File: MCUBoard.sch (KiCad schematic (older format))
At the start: 25 parts

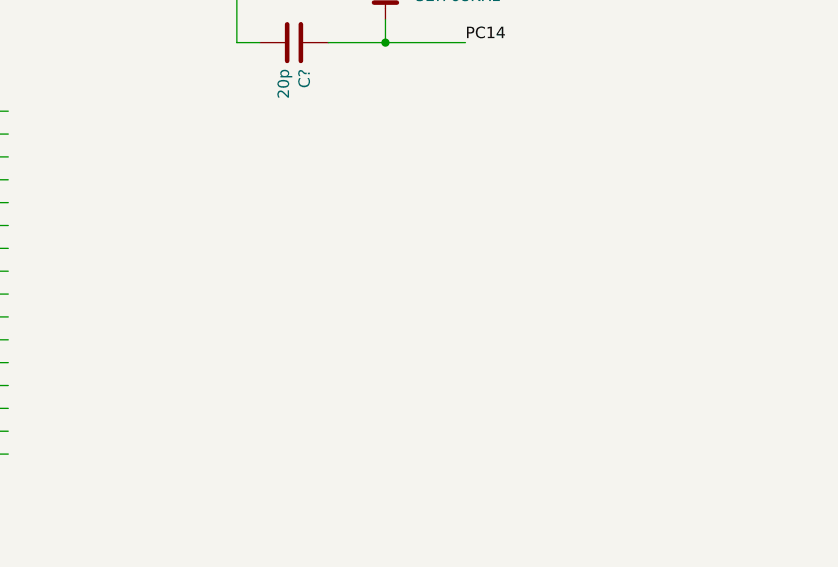
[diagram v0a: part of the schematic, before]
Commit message: added LDO to convert 5v to 3.3v
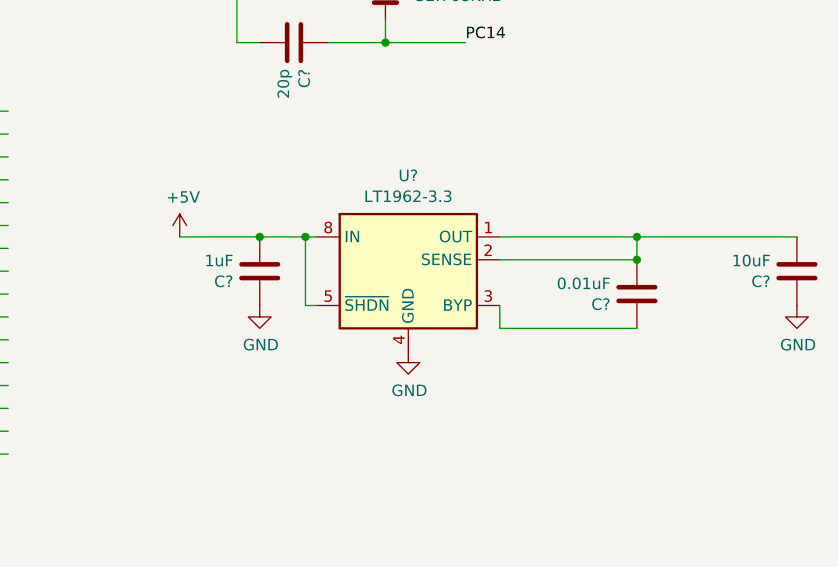
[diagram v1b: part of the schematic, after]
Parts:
- added C?: 0.01uF, symbol Device:C
- added C?: 10uF, symbol Device:C
- added C?: 1uF, symbol Device:C
- added U?: LT1962-3.3, Package_SO:MSOP-8_3x3mm_P0.65mm, symbol Regulator_Linear:LT1962-3.3
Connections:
- wire segments 105 -> 116
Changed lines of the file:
@@
 Wire Wire Line
 	1150 6400 1700 6400
+$Comp
+L Regulator_Linear:LT1962-3.3 U?
+U 1 1 5BB1DF66
+P 8250 3950
+F 0 "U?" H 8250 4417 50  0000 C CNN
+F 1 "LT1962-3.3" H 8250 4326 50  0000 C CNN
+F 2 "Package_SO:MSOP-8_3x3mm_P0.65mm" H 8250 3600 50  0001 C CNN
+F 3 "http://cds.linear.com/docs/en/datasheet/1962fb.pdf" H 8250 3400 50  0001 C CNN
+	1    8250 3950
+	1    0    0    -1
+$EndComp
+$Comp
+L Device:C C?
+U 1 1 5BB1E1BB
+P 9250 4000
+F 0 "C?" H 9365 4046 50  0000 L CNN
+F 1 "0.01uF" H 9365 3955 50  0000 L CNN
+F 2 "" H 9288 3850 50  0001 C CNN
+F 3 "~" H 9250 4000 50  0001 C CNN
+	1    9250 4000
+	-1   0    0    1
+$EndComp
+$Comp
+L Device:C C?
+U 1 1 5BB1E331
+P 9950 3900
+F 0 "C?" H 10065 3946 50  0000 L CNN
+F 1 "10uF" H 10065 3855 50  0000 L CNN
+F 2 "" H 9988 3750 50  0001 C CNN
+F 3 "~" H 9950 3900 50  0001 C CNN
+	1    9950 3900
+	-1   0    0    1
+$EndComp
+$Comp
+L Device:C C?
+U 1 1 5BB1E3E9
+P 7600 3900
+F 0 "C?" H 7715 3946 50  0000 L CNN
+F 1 "1uF" H 7715 3855 50  0000 L CNN
+F 2 "" H 7638 3750 50  0001 C CNN
+F 3 "~" H 7600 3900 50  0001 C CNN
+	1    7600 3900
+	-1   0    0    1
+$EndComp
+Wire Wire Line
+	7850 3750 7800 3750
+Connection ~ 7600 3750
+Wire Wire Line
+	7600 3750 7250 3750
+Wire Wire Line
+	7850 4050 7800 4050
+Wire Wire Line
+	7800 4050 7800 3750
+Connection ~ 7800 3750
+Wire Wire Line
+	7800 3750 7600 3750
+Wire Wire Line
+	9250 4150 8650 4150
+Wire Wire Line
+	8650 4150 8650 4050
+Wire Wire Line
+	8650 3850 9250 3850
+Wire Wire Line
+	9250 3750 9250 3850
+Wire Wire Line
+	8650 3750 9250 3750
+Connection ~ 9250 3850
+Wire Wire Line
+	9250 3750 9950 3750
+Connection ~ 9250 3750
+$Comp
+L power:GND #PWR?
+U 1 1 5BB3BDE6
+P 8250 4250
+F 0 "#PWR?" H 8250 4000 50  0001 C CNN
+F 1 "GND" H 8255 4077 50  0000 C CNN
+F 2 "" H 8250 4250 50  0001 C CNN
+F 3 "" H 8250 4250 50  0001 C CNN
+	1    8250 4250
+	1    0    0    -1
+$EndComp
+$Comp
+L power:GND #PWR?
+U 1 1 5BB3BE2B
+P 7600 4050
+F 0 "#PWR?" H 7600 3800 50  0001 C CNN
+F 1 "GND" H 7605 3877 50  0000 C CNN
+F 2 "" H 7600 4050 50  0001 C CNN
+F 3 "" H 7600 4050 50  0001 C CNN
+	1    7600 4050
+	1    0    0    -1
+$EndComp
+$Comp
+L power:GND #PWR?
+U 1 1 5BB3BE70
+P 9950 4050
+F 0 "#PWR?" H 9950 3800 50  0001 C CNN
+F 1 "GND" H 9955 3877 50  0000 C CNN
+F 2 "" H 9950 4050 50  0001 C CNN
+F 3 "" H 9950 4050 50  0001 C CNN
+	1    9950 4050
+	1    0    0    -1
+$EndComp
+$Comp
+L power:+5V #PWR?
+U 1 1 5BB3C133
+P 7250 3750
+F 0 "#PWR?" H 7250 3600 50  0001 C CNN
+F 1 "+5V" H 7265 3923 50  0000 C CNN
+F 2 "" H 7250 3750 50  0001 C CNN
+F 3 "" H 7250 3750 50  0001 C CNN
+	1    7250 3750
+	1    0    0    -1
+$EndComp
 $EndSCHEMATC

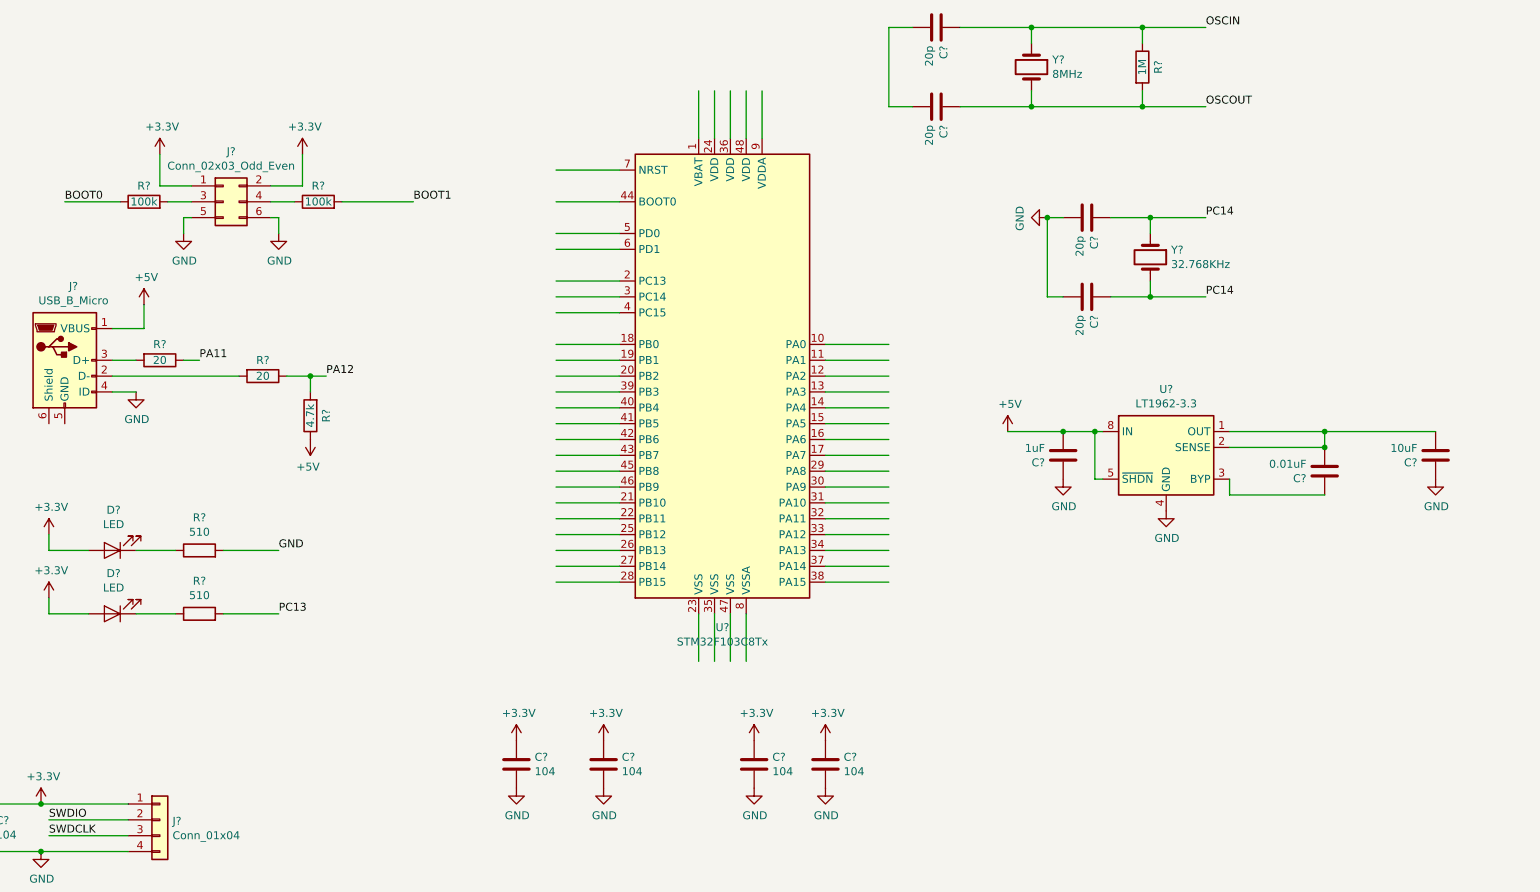
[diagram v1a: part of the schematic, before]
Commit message: label mcu and connect power
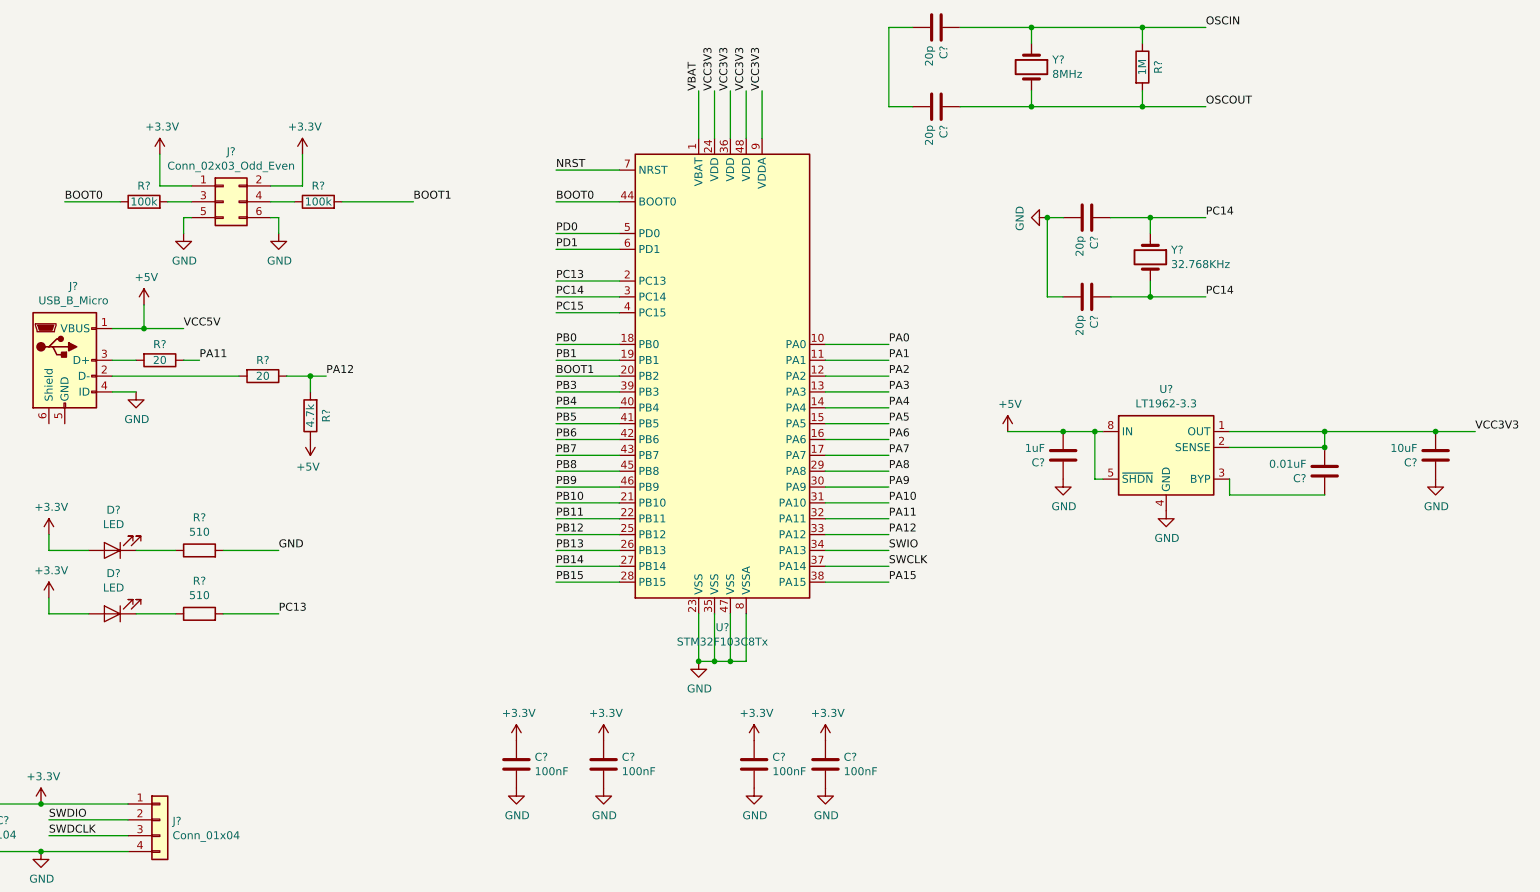
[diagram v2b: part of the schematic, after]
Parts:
- C? (x4): value 104 -> 100nF
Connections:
- net labels added: NRST, PA0, PA1, PA10, PA15, PA2, PA3, PA4, PA5, PA6, PA7, PA8, PA9, PB0, PB1, PB10, PB11, PB12, PB13, PB14, PB15, PB3, PB4, PB5, PB6, PB7, PB8, PB9, PC15, PD0, PD1, SWCLK, SWIO, VBAT, VCC3V3, VCC5V
- wire segments 116 -> 121
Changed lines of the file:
@@
 EELAYER 26 0
 EELAYER END
-$Descr A4 11693 8268
+$Descr B 17000 11000
 encoding utf-8
 Sheet 1 1
@@
 Wire Wire Line
 	1800 2950 1800 3100
-Wire Wire Line
-	1800 3100 1600 3100
 $Comp
 L Device:R R?
@@
 P 4150 5850
 F 0 "C?" H 4265 5896 50  0000 L CNN
-F 1 "104" H 4265 5805 50  0000 L CNN
+F 1 "100nF" H 4265 5805 50  0000 L CNN
 F 2 "" H 4188 5700 50  0001 C CNN
 F 3 "~" H 4150 5850 50  0001 C CNN
@@
 P 4700 5850
 F 0 "C?" H 4815 5896 50  0000 L CNN
-F 1 "104" H 4815 5805 50  0000 L CNN
+F 1 "100nF" H 4815 5805 50  0000 L CNN
 F 2 "" H 4738 5700 50  0001 C CNN
 F 3 "~" H 4700 5850 50  0001 C CNN
@@
 P 5650 5850
 F 0 "C?" H 5765 5896 50  0000 L CNN
-F 1 "104" H 5765 5805 50  0000 L CNN
+F 1 "100nF" H 5765 5805 50  0000 L CNN
 F 2 "" H 5688 5700 50  0001 C CNN
 F 3 "~" H 5650 5850 50  0001 C CNN
@@
 P 6100 5850
 F 0 "C?" H 6215 5896 50  0000 L CNN
-F 1 "104" H 6215 5805 50  0000 L CNN
+F 1 "100nF" H 6215 5805 50  0000 L CNN
 F 2 "" H 6138 5700 50  0001 C CNN
 F 3 "~" H 6100 5850 50  0001 C CNN
@@
 	1    0    0    -1
 $EndComp
+Text Label 6500 3200 0    50   ~ 0
+PA0
+Text Label 6500 3300 0    50   ~ 0
+PA1
+Text Label 6500 3400 0    50   ~ 0
+PA2
+Text Label 6500 3500 0    50   ~ 0
+PA3
+Text Label 6500 3600 0    50   ~ 0
+PA4
+Text Label 6500 3700 0    50   ~ 0
+PA5
+Text Label 6500 3800 0    50   ~ 0
+PA6
+Text Label 6500 3900 0    50   ~ 0
+PA7
+Text Label 6500 4000 0    50   ~ 0
+PA8
+Text Label 6500 4100 0    50   ~ 0
+PA9
+Text Label 6500 4200 0    50   ~ 0
+PA10
+Text Label 6500 4300 0    50   ~ 0
+PA11
+Text Label 6500 4400 0    50   ~ 0
+PA12
+Text Label 6500 4500 0    50   ~ 0
+SWIO
+Text Label 6500 4600 0    50   ~ 0
+SWCLK
+Text Label 6500 4700 0    50   ~ 0
+PA15
+Text Label 4400 2100 0    50   ~ 0
+NRST
+Text Label 4400 2300 0    50   ~ 0
+BOOT0
+Text Label 4400 2500 0    50   ~ 0
+PD0
+Text Label 4400 2600 0    50   ~ 0
+PD1
+Text Label 4400 2800 0    50   ~ 0
+PC13
+Text Label 4400 2900 0    50   ~ 0
+PC14
+Text Label 4400 3000 0    50   ~ 0
+PC15
+Text Label 4400 3200 0    50   ~ 0
+PB0
+Text Label 4400 3300 0    50   ~ 0
+PB1
+Text Label 4400 3400 0    50   ~ 0
+BOOT1
+Text Label 4400 3500 0    50   ~ 0
+PB3
+Text Label 4400 3600 0    50   ~ 0
+PB4
+Text Label 4400 3700 0    50   ~ 0
+PB5
+Text Label 4400 3800 0    50   ~ 0
+PB6
+Text Label 4400 3900 0    50   ~ 0
+PB7
+Text Label 4400 4000 0    50   ~ 0
+PB8
+Text Label 4400 4100 0    50   ~ 0
+PB9
+Text Label 4400 4200 0    50   ~ 0
+PB10
+Text Label 4400 4300 0    50   ~ 0
+PB11
+Text Label 4400 4400 0    50   ~ 0
+PB12
+Text Label 4400 4500 0    50   ~ 0
+PB13
+Text Label 4400 4600 0    50   ~ 0
+PB14
+Text Label 4400 4700 0    50   ~ 0
+PB15
+Wire Wire Line
+	1600 3100 1800 3100
+Wire Wire Line
+	1800 3100 2050 3100
+Connection ~ 1800 3100
+Text Label 2050 3100 0    50   ~ 0
+VCC5V
+Wire Wire Line
+	9950 3750 10200 3750
+Connection ~ 9950 3750
+Text Label 10200 3750 0    50   ~ 0
+VCC3V3
+Text Label 5300 1600 1    50   ~ 0
+VBAT
+Text Label 5400 1600 1    50   ~ 0
+VCC3V3
+Text Label 5500 1600 1    50   ~ 0
+VCC3V3
+Text Label 5600 1600 1    50   ~ 0
+VCC3V3
+Text Label 5700 1600 1    50   ~ 0
+VCC3V3
+$Comp
+L power:GND #PWR?
+U 1 1 5BB4C12D
+P 5300 5200
+F 0 "#PWR?" H 5300 4950 50  0001 C CNN
+F 1 "GND" H 5305 5027 50  0000 C CNN
+F 2 "" H 5300 5200 50  0001 C CNN
+F 3 "" H 5300 5200 50  0001 C CNN
+	1    5300 5200
+	1    0    0    -1
+$EndComp
+Wire Wire Line
+	5300 5200 5400 5200
+Connection ~ 5300 5200
+Connection ~ 5400 5200
+Wire Wire Line
+	5400 5200 5500 5200
+Connection ~ 5500 5200
+Wire Wire Line
+	5500 5200 5600 5200
 $EndSCHEMATC
